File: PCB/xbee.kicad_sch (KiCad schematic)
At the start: 9 parts

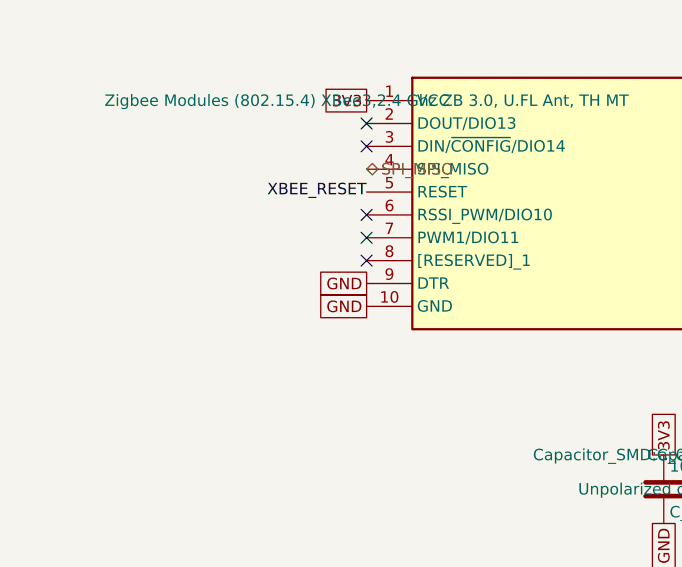
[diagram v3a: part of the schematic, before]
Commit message: Accelerometer-driven low-power mode (hardware, PCB only) (#47)
* feat: accelerometer-driven low-power mode (hardware, PCB 1/2)

Adds a QMA6100P accelerometer (I2C, shared OLED bus) and enables
host-commanded XBee pin-sleep, laying the hardware groundwork for a
low-power mode: OLED off + XBee sleep after a short idle timeout (no
buttons, no motion), full soft-latch power-off after a longer one.

- QMA6100P chosen after checking JLCPCB's actual parts library: no
  candidate accelerometer is Basic-library, so it won on price, size,
  and standby current (500nA), which matters since it has to watch for
  motion through the whole low-power period.
- Hand-authored symbol + footprint (no existing library part) — pad
  geometry pulled from JLCPCB/LCSC's own EasyEDA component data
  (LCSC C2887190), not estimated from the datasheet's low-res drawing.
- New Accelerometer sheet, wired into the existing I2C bus and into a
  new GPIO46 (INT1) interrupt line so the MCU can light-sleep instead
  of polling for wake conditions.
- XBee DTR moved off its permanent GND tie onto GPIO42 (SLEEP_RQ), so
  firmware can actually request/cancel pin-sleep instead of the radio
  being forced awake at all times.
- Placed, routed, DRC- and ERC-clean.

Firmware (driver, low-power state machine) and production file
generation are follow-up work — this PR is hardware/schematic only.

Co-Authored-By: Claude Sonnet 5 <noreply@anthropic.com>

* feat: accelerometer-driven low-power mode (firmware, PCB 2/2)

Progressive-enhancement low-power mode: idle cascade through
full -> dim OLED -> OLED off -> XBee sleep (each stage independently
timed, capped by a configurable aggressiveness mode), plus an
independent auto-poweroff timer that fires regardless of mode.

- PowerManager (power_management.h/.cpp): pure, unit-tested state
  machine. Takes "did anything happen this tick" and current time,
  reports which tier to be in and a one-shot poweroff flag. No
  capability flags needed for progressive enhancemen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
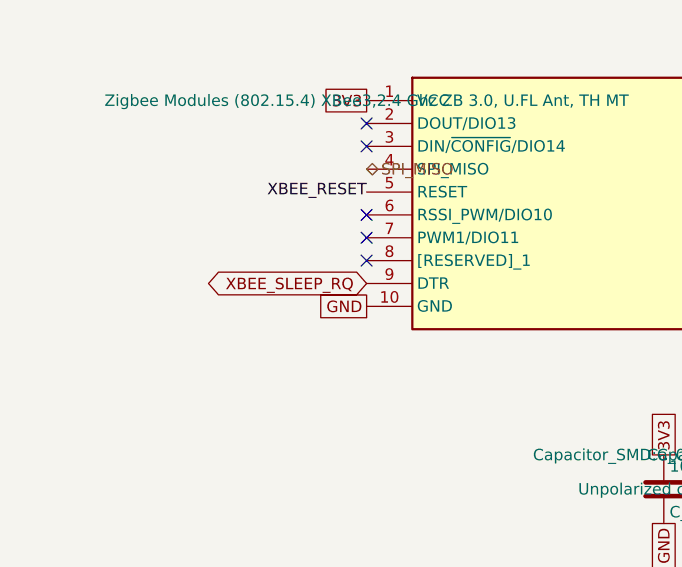
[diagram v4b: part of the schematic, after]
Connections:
- net GND: no longer U_XBEE1.9 (DTR)
- new net XBEE_SLEEP_RQ: U_XBEE1.9 (DTR)
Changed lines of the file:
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@@
+	(global_label "3V3"
+		(shape passive)
+		(at 101.6 96.52 180)
+		(fields_autoplaced yes)
+		(effects
+			(font
+				(size 1.27 1.27)
+			)
+			(justify right)
+		)
+		(property "Intersheetrefs" "${INTERSHEET_REFS}"
+			(at 101.6 96.52 0)
+			(hide yes)
+			(show_name no)
+			(do_not_autoplace no)
+			(effects
+				(font
+					(size 1.27 1.27)
+				)
+			)
+		)
+	)
 	(global_label "3V3"
 		(shape passive)
@@
 		)
 	)
-	(global_label "3V3"
-		(shape passive)
-		(at 101.6 96.52 180)
-		(fields_autoplaced yes)
-		(effects
-			(font
-				(size 1.27 1.27)
-			)
-			(justify right)
-		)
-		(property "Intersheetrefs" "${INTERSHEET_REFS}"
-			(at 101.6 96.52 0)
-			(hide yes)
-			(show_name no)
-			(do_not_autoplace no)
-			(effects
-				(font
-					(size 1.27 1.27)
-				)
-			)
-		)
-	)
 	(global_label "GND"
 		(shape passive)
@@
 		)
 	)
-	(global_label "GND"
-		(shape passive)
-		(at 101.6 116.84 180)
-		(fields_autoplaced yes)
-		(effects
-			(font
-				(size 1.27 1.27)
-			)
-			(justify right)
-		)
-		(property "Intersheetrefs" "${INTERSHEET_REFS}"
-			(at 101.6 116.84 0)
-			(hide yes)
-			(show_name no)
-			(do_not_autoplace no)
-			(effects
-				(font
-					(size 1.27 1.27)
-				)
-			)
-		)
-	)
 	(global_label "3V3"
 		(shape passive)
@@
 		(property "Intersheetrefs" "${INTERSHEET_REFS}"
 			(at 172.72 135.89 0)
+			(hide yes)
+			(show_name no)
+			(do_not_autoplace no)
+			(effects
+				(font
+					(size 1.27 1.27)
+				)
+			)
+		)
+	)
+	(global_label "XBEE_SLEEP_RQ"
+		(shape bidirectional)
+		(at 101.6 116.84 180)
+		(fields_autoplaced yes)
+		(effects
+			(font
+				(size 1.27 1.27)
+			)
+			(justify right)
+		)
+		(property "Intersheetrefs" "${INTERSHEET_REFS}"
+			(at 101.6 116.84 0)
 			(hide yes)
 			(show_name no)
@@
 	(symbol
 		(lib_id "Device:R")
+		(at 166.37 69.85 0)
+		(unit 1)
+		(body_style 1)
+		(exclude_from_sim no)
+		(in_bom yes)
+		(on_board yes)
+		(in_pos_files yes)
+		(dnp no)
+		(fields_autoplaced yes)
+		(property "Reference" "R_XBEE_RC1"
+			(at 168.402 69.85 90)
+			(show_name no)
+			(do_not_autoplace no)
+			(effects
+				(font
+					(size 1.27 1.27)
+				)
+			)
+		)
+		(property "Value" "100Ω"
+			(at 166.37 69.85 90)
+			(show_name no)
+			(do_not_autoplace no)
+			(effects
+				(font
+					(size 1.27 1.27)
+				)
+			)
+		)
+		(property "Footprint" "Resistor_SMD:R_0402_1005Metric"
+			(at 164.592 69.85 90)
+			(show_name no)
+			(do_not_autoplace no)
+			(effects
+				(font
+					(size 1.27 1.27)
+				)
+			)
+		)
+		(property "Datasheet" ""
+			(at 166.37 69.85 0)
+			(show_name no)
+			(do_not_autoplace no)
+			(effects
+				(font
+					(size 1.27 1.27)
+				)
+			)
+		)
+		(property "Description" "Resistor"
+			(at 166.37 69.85 0)
+			(show_name no)
+			(do_not_autoplace no)
+			(effects
+				(font
+					(size 1.27 1.27)
+				)
+			)
+		)
+		(property "MF" "UNI-ROYAL(Uniroyal Elec)"
+			(at 0 0 0)
+			(hide yes)
+			(show_name no)
+			(do_not_autoplace no)
+			(effects
+				(font
+					(size 1.27 1.27)
+				)
+			)
+		)
+		(property "Manufacturer_Part_Number" "0402WGF1000TCE"
+			(at 0 0 0)
+			(hide yes)
+			(show_name no)
+			(do_not_autoplace no)
+			(effects
+				(font
+					(size 1.27 1.27)
+				)
+			)
+		)
+		(property "LCSC" "C25076"
+			(at 0 0 0)
+			(hide yes)
+			(show_name no)
+			(do_not_autoplace no)
+			(effects
+				(font
+					(size 1.27 1.27)
+				)
+			)
+		)
+		(pin "1"
+		)
+		(pin "2"
+		)
+		(instances
+			(project "snips_controller"
+				(path "/21935953-32a0-46ad-8079-8177920c6978/4f95850f-f8fc-4b0b-b598-e710af0bb56d"
+					(reference "R_XBEE_RC1")
+					(unit 1)
+				)
+			)
+		)
+	)
+	(symbol
+		(lib_id "Device:R")
 		(at 210.82 110.49 0)
 		(unit 1)
@@
 					(unit 1)
 				)
-			)
-		)
-	)
-	(symbol
-		(lib_id "Device:R")
-		(at 166.37 69.85 0)
-		(unit 1)
-		(body_style 1)
-		(exclude_from_sim no)
-		(in_bom yes)
-		(on_board yes)
-		(in_pos_files yes)
-		(dnp no)
-		(fields_autoplaced yes)
-		(property "Reference" "R_XBEE_RC1"
-			(at 168.402 69.85 90)
-			(show_name no)
-			(do_not_autoplace no)
-			(effects
-				(font
-					(size 1.27 1.27)
-				)
-			)
-		)
-		(property "Value" "100Ω"
-			(at 166.37 69.85 90)
-			(show_name no)
-			(do_not_autoplace no)
-			(effects
-				(font
-					(size 1.27 1.27)
-				)
-			)
-		)
-		(property "Footprint" "Resistor_SMD:R_0402_1005Metric"
-			(at 164.592 69.85 90)
-			(show_name no)
-			(do_not_autoplace no)
-			(effects
-				(font
-					(size 1.27 1.27)
-				)
-			)
-		)
-		(property "Datasheet" ""
-			(at 166.37 69.85 0)
-			(show_name no)
-			(do_not_autoplace no)
-			(effects
-				(font
-					(size 1.27 1.27)
-				)
-			)
-		)
-		(property "Description" "Resistor"
-			(at 166.37 69.85 0)
-			(show_name no)
-			(do_not_autoplace no)
-			(effects
-				(font
-					(size 1.27 1.27)
-				)
-			)
-		)
-		(property "MF" "UNI-ROYAL(Uniroyal Elec)"
-			(at 0 0 0)
-			(hide yes)
-			(show_name no)
-			(do_not_autoplace no)
-			(effects
-				(font
-					(size 1.27 1.27)
-				)
-			)
-		)
-		(property "Manufacturer_Part_Number" "0402WGF1000TCE"
-			(at 0 0 0)
-			(hide yes)
-			(show_name no)
-			(do_not_autoplace no)
-			(effects
-				(font
-					(size 1.27 1.27)
-				)
-			)
-		)
-		(property "LCSC" "C25076"
-			(at 0 0 0)
-			(hide yes)
-			(show_name no)
-			(do_not_autoplace no)
-			(effects
-				(font
-					(size 1.27 1.27)
-				)
-			)
-		)
-		(pin "1"
-		)
-		(pin "2"
-		)
-		(instances
-			(project "snips_controller"
-				(path "/21935953-32a0-46ad-8079-8177920c6978/4f95850f-f8fc-4b0b-b598-e710af0bb56d"
-					(reference "R_XBEE_RC1")
-					(unit 1)
-				)

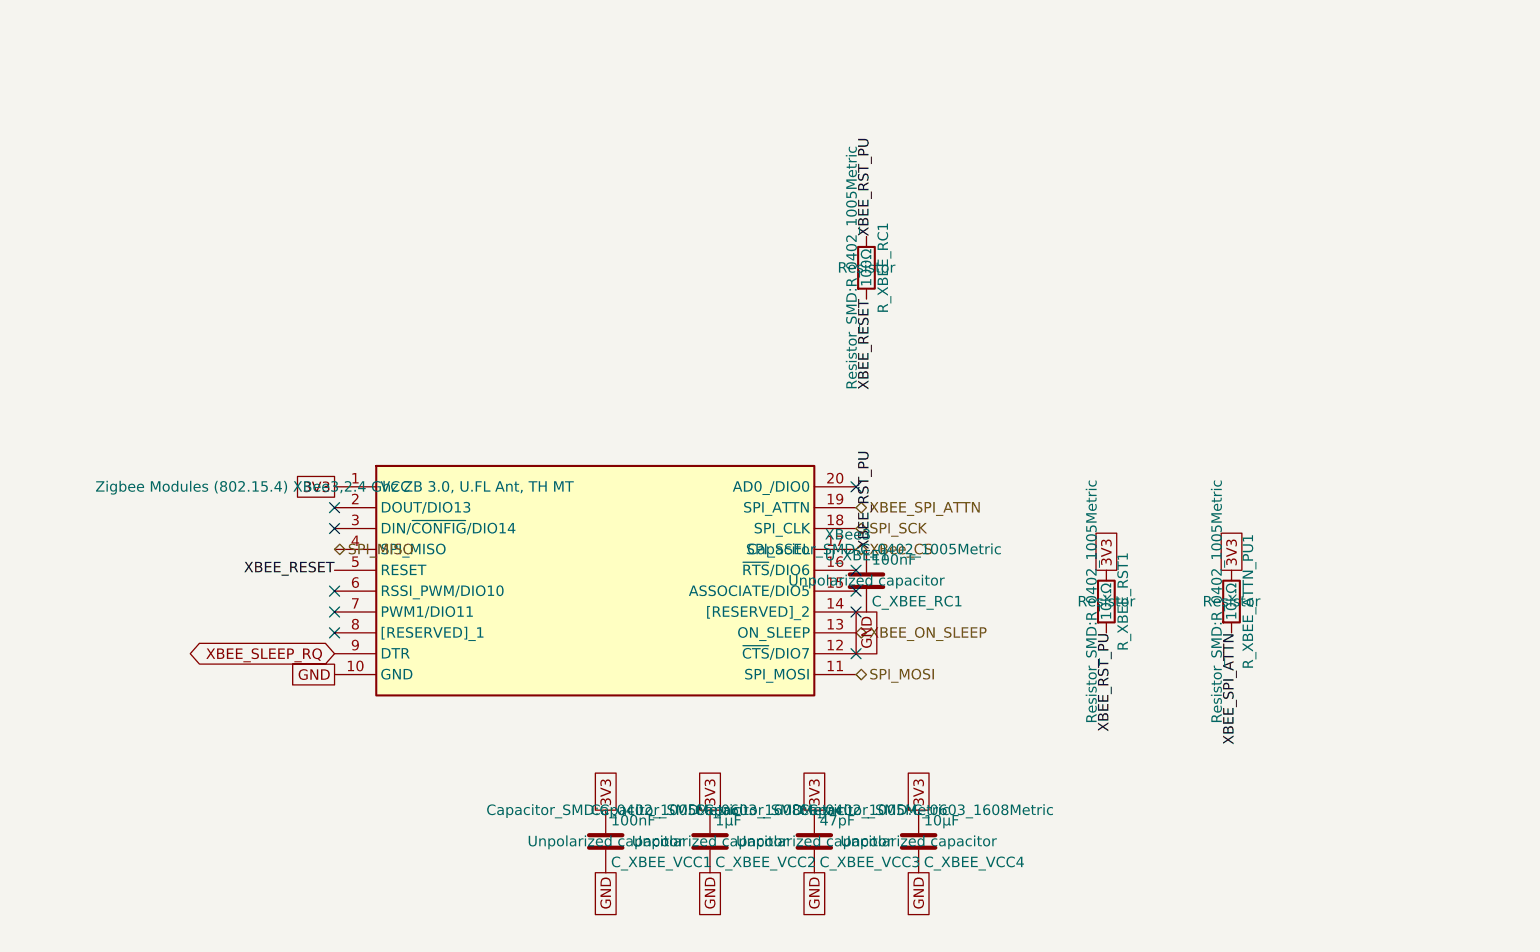
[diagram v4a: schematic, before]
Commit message: fix: make every BOM Value unambiguous for the fab, and switch D_INV_ISO1 to SOT-323 (#61)
* fix: make every BOM Value unambiguous for the fab, and switch D_INV_ISO1 to SOT-323

PCBWay flagged D_INV_ISO1: "BAT54W" is SOT-323 from nearly every maker, but we
had picked Yangjie's SOD-123 variant. A fab only sees Designator, Footprint,
Quantity and Value in the BOM (never MF/MPN/LCSC), so a bare part name is
ambiguous. Fixes the class of problem, not just this part:

- Every component's Value is now "<label> | <MPN> | <manufacturer> | <package>"
  (label dropped when it repeats the MPN; commas/periods stripped so the CSV
  never needs quoting). BT1 keeps its RIGHT-ANGLE HORIZONTAL note. Applied to
  all 81 parts across every sheet and the PCB.
- scripts/bom_values.py builds, applies, and checks these values, including
  that the PCB copy of Value/MF/MPN/footprint matches the schematic. New
  footprints must be added to its package table on purpose; hand-sourced parts
  with no MPN (J_STICK1) are listed explicitly.
- D_INV_ISO1 -> Diodes BAT54W-7-F in SOT-323 (common part, several makers).
  Pin 1 anode / pin 2 not connected / pin 3 cathode, confirmed against
  Nexperia's numbered pinning table and Diodes' datasheet. Uses KiCad's
  Diode:BAT54W symbol; PCB footprint replaced and rerouted. Electrically the
  same BAT54 family (30V, 200mA, 2uA leakage at 25V), so the SPICE model and
  scripts/spice/latch_sim.py still pass.
- Layout diagrams now say AO3401A for Q_PWR1 (they were stale since it was
  swapped from DMG2305UX) and BAT54W-7-F/SOT-323 for D_INV_ISO1.
- Repo CLAUDE.md documents the Value rule and the script.

ERC/DRC clean; production files regenerated.

Co-Authored-By: Claude Sonnet 5 <noreply@anthropic.com>

* chore: commit KiCad project settings (reordered used-designators list)

Co-Authored-By: Claude Sonnet 5 <noreply@anthropic.com>

---------

Co-authored-by: Claude Sonnet 5 <noreply@anthropic.com>
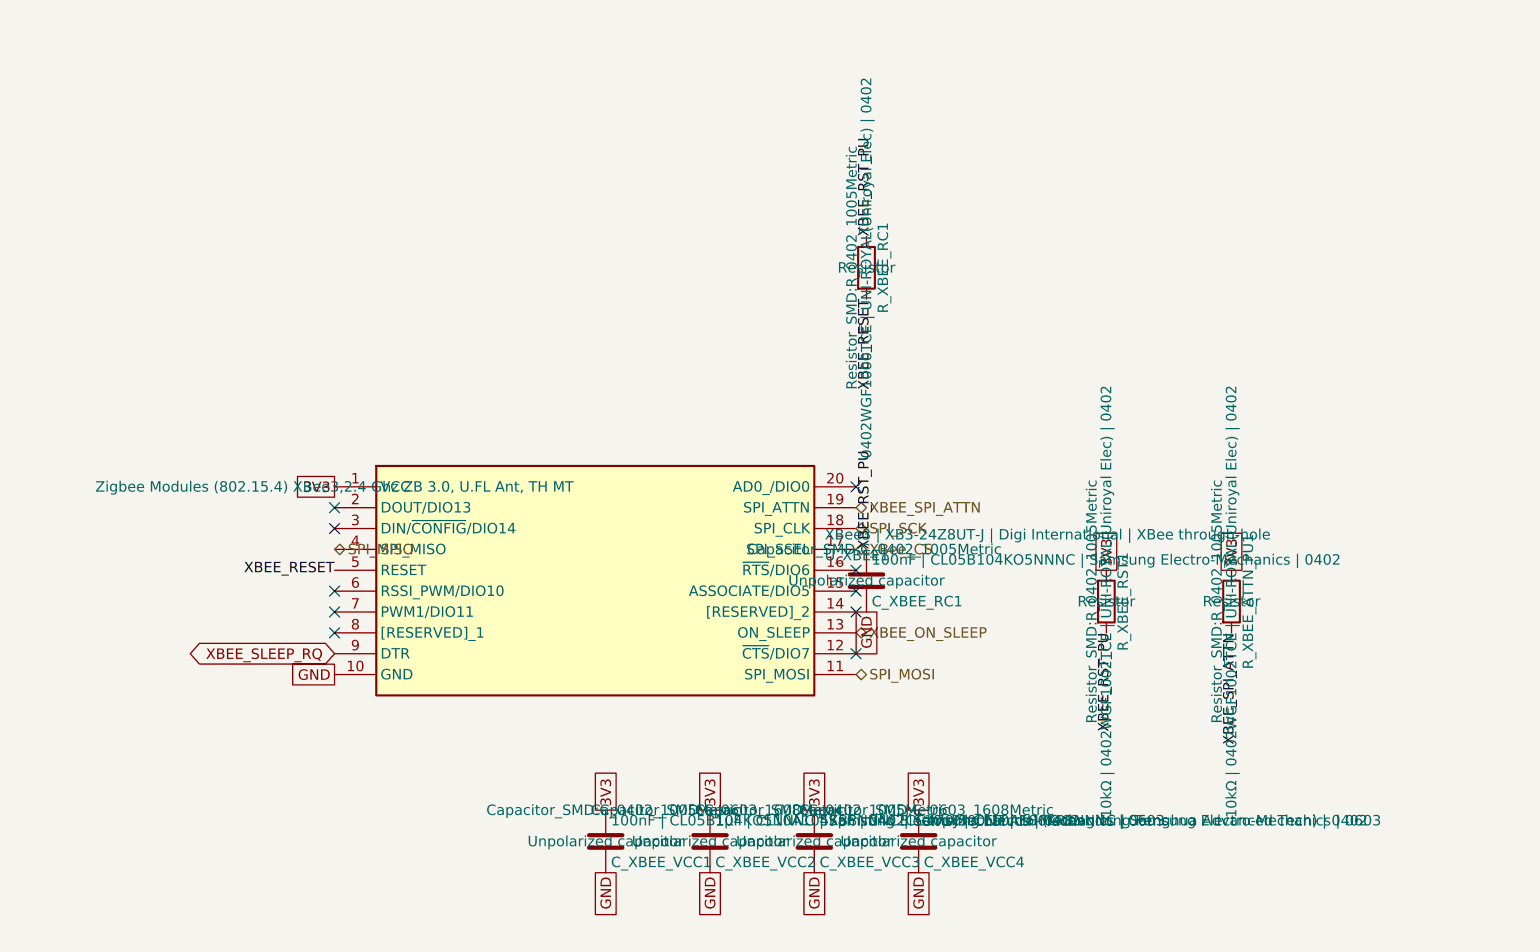
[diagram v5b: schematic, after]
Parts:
- C_XBEE_RC1, C_XBEE_VCC1: value 100nF -> 100nF | CL05B104KO5NNNC | Samsung Electro-Mechanics | 0402
- C_XBEE_VCC2: value 1µF -> 1µF | CL10A105KB8NNNC | Samsung Electro-Mechanics | 0603
- C_XBEE_VCC3: value 47pF -> 47pF | 0402CG470J500NT | FH (Guangdong Fenghua Advanced Tech) | 0402
- C_XBEE_VCC4: value 10µF -> 10µF | CL10A106KP8NNNC | Samsung Electro-Mechanics | 0603
- R_XBEE_ATTN_PU1, R_XBEE_RST1: value 10kΩ -> 10kΩ | 0402WGF1002TCE | UNI-ROYAL(Uniroyal Elec) | 0402
- R_XBEE_RC1: value 100Ω -> 0402WGF1000TCE | UNI-ROYAL(Uniroyal Elec) | 0402
- U_XBEE1: value XBee3 -> XBee3 | XB3-24Z8UT-J | Digi International | XBee through-hole
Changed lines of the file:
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@@
 			)
 		)
-		(property "Value" "47pF"
+		(property "Value" "47pF | 0402CG470J500NT | FH (Guangdong Fenghua Advanced Tech) | 0402"
 			(at 160.655 137.16 0)
 			(show_name no)
@@
 			)
 		)
-		(property "Value" "XBee3"
+		(property "Value" "XBee3 | XB3-24Z8UT-J | Digi International | XBee through-hole"
 			(at 161.29 101.6 0)
 			(show_name no)
@@
 			)
 		)
-		(property "Value" "1µF"
+		(property "Value" "1µF | CL10A105KB8NNNC | Samsung Electro-Mechanics | 0603"
 			(at 147.955 137.16 0)
 			(show_name no)
@@
 			)
 		)
-		(property "Value" "10µF"
+		(property "Value" "10µF | CL10A106KP8NNNC | Samsung Electro-Mechanics | 0603"
 			(at 173.355 137.16 0)
 			(show_name no)
@@
 			)
 		)
-		(property "Value" "100nF"
+		(property "Value" "100nF | CL05B104KO5NNNC | Samsung Electro-Mechanics | 0402"
 			(at 167.005 105.41 0)
 			(show_name no)
@@
 			)
 		)
-		(property "Value" "10kΩ"
+		(property "Value" "10kΩ | 0402WGF1002TCE | UNI-ROYAL(Uniroyal Elec) | 0402"
 			(at 195.58 110.49 90)
 			(show_name no)
@@
 			)
 		)
-		(property "Value" "100Ω"
+		(property "Value" "0402WGF1000TCE | UNI-ROYAL(Uniroyal Elec) | 0402"
 			(at 166.37 69.85 90)
 			(show_name no)
@@
 			)
 		)
-		(property "Value" "10kΩ"
+		(property "Value" "10kΩ | 0402WGF1002TCE | UNI-ROYAL(Uniroyal Elec) | 0402"
 			(at 210.82 110.49 90)
 			(show_name no)
@@
 			)
 		)
-		(property "Value" "100nF"
+		(property "Value" "100nF | CL05B104KO5NNNC | Samsung Electro-Mechanics | 0402"
 			(at 135.255 137.16 0)
 			(show_name no)
